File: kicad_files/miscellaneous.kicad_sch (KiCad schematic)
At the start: 28 parts, among them J2 TYPE-C-31-M-12, Q1 DTC123JKAT146, SW1 SW_SPST, SW2 EC11, U2 USBLC6-2SC6, U3 MCP1700-3302E

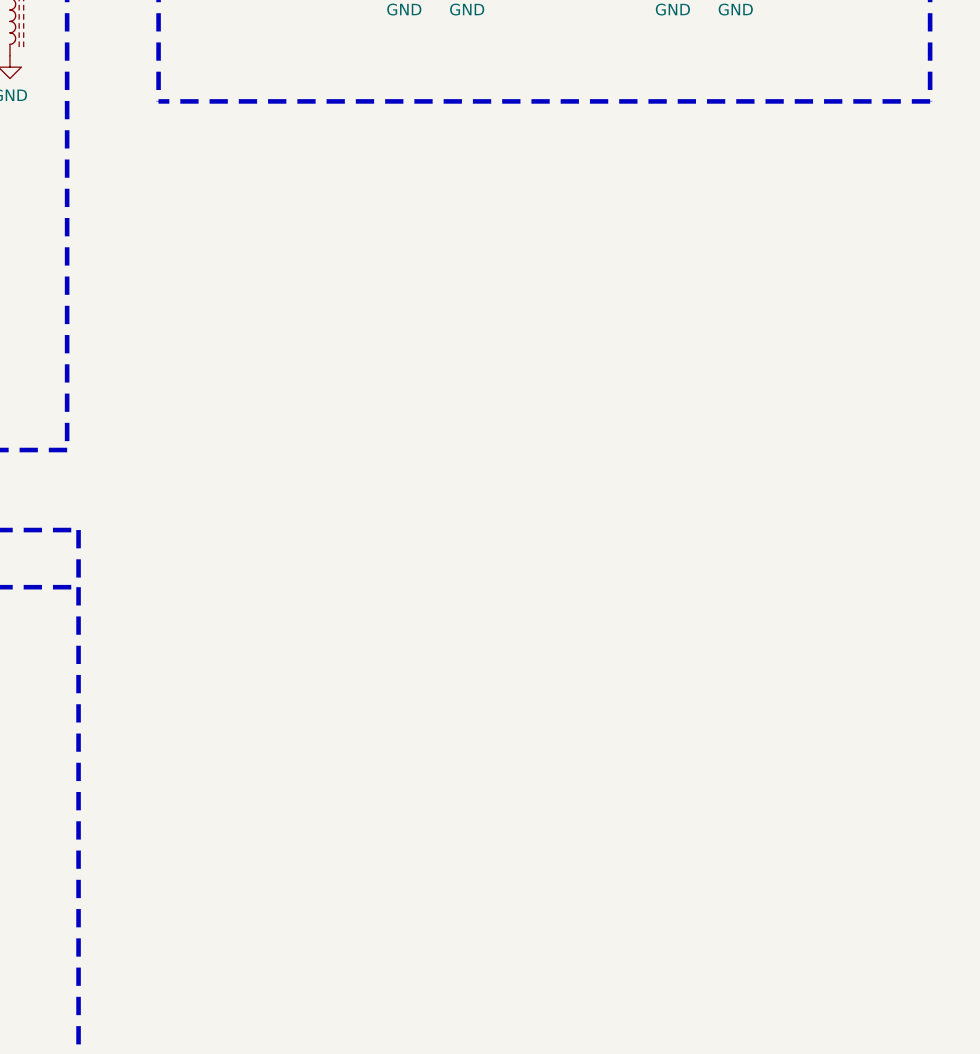
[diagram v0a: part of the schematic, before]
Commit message: Added mounting holes and jst connector
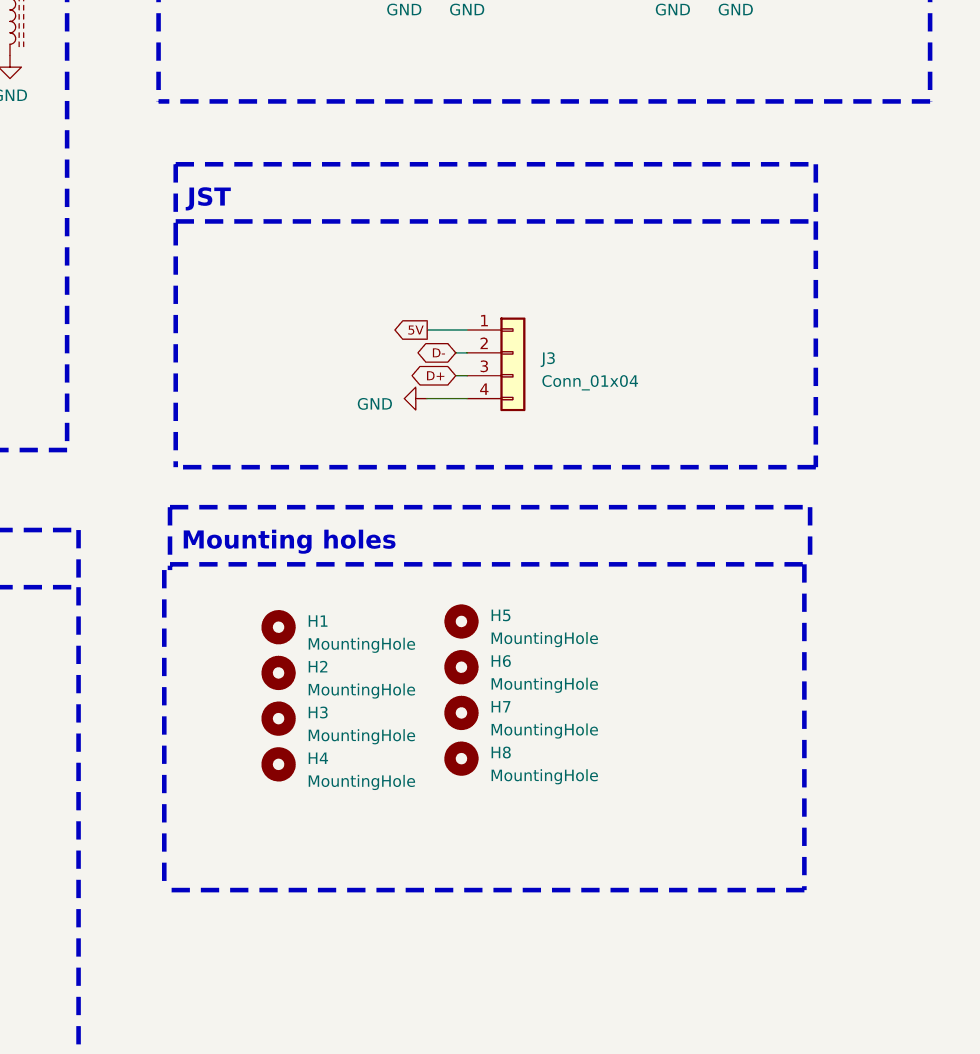
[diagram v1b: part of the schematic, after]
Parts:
- added H1, H2, H3, H4: MountingHole, acheron_MountingHoles:MountingHole_2.5x4.0mm, symbol Mechanical:MountingHole
- added H5, H6, H7, H8: MountingHole, acheron_MountingHoles:MoutingHole_Oval_7mm_5.0x2.5mm, symbol Mechanical:MountingHole
- added J3: Conn_01x04, acheron_Connectors:SM04B-SRSS-TB(LF)(SN)_mounting-reliefs, symbol Connector_Generic:Conn_01x04
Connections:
- net 5V: now also J3.1 (Pin_1)
- net D+: now also J3.3 (Pin_3)
- net D-: now also J3.2 (Pin_2)
- net GND: now also J3.4 (Pin_4)
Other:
- note added: "JST"
- note added: "Mounting holes"

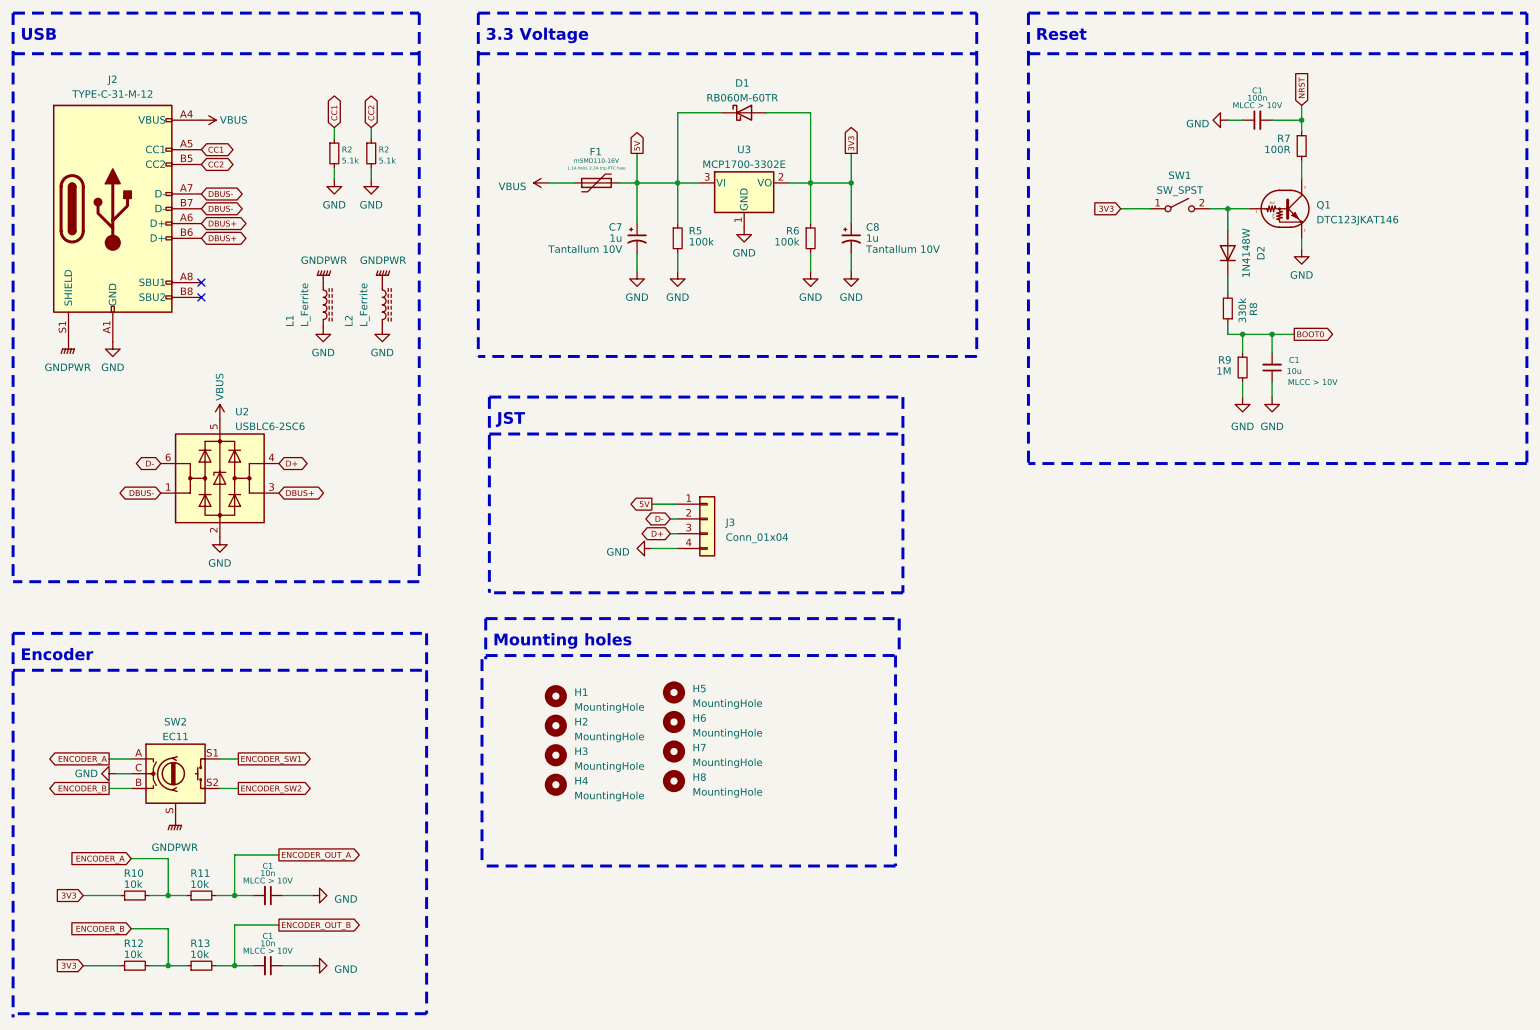
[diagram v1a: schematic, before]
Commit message: Added oled
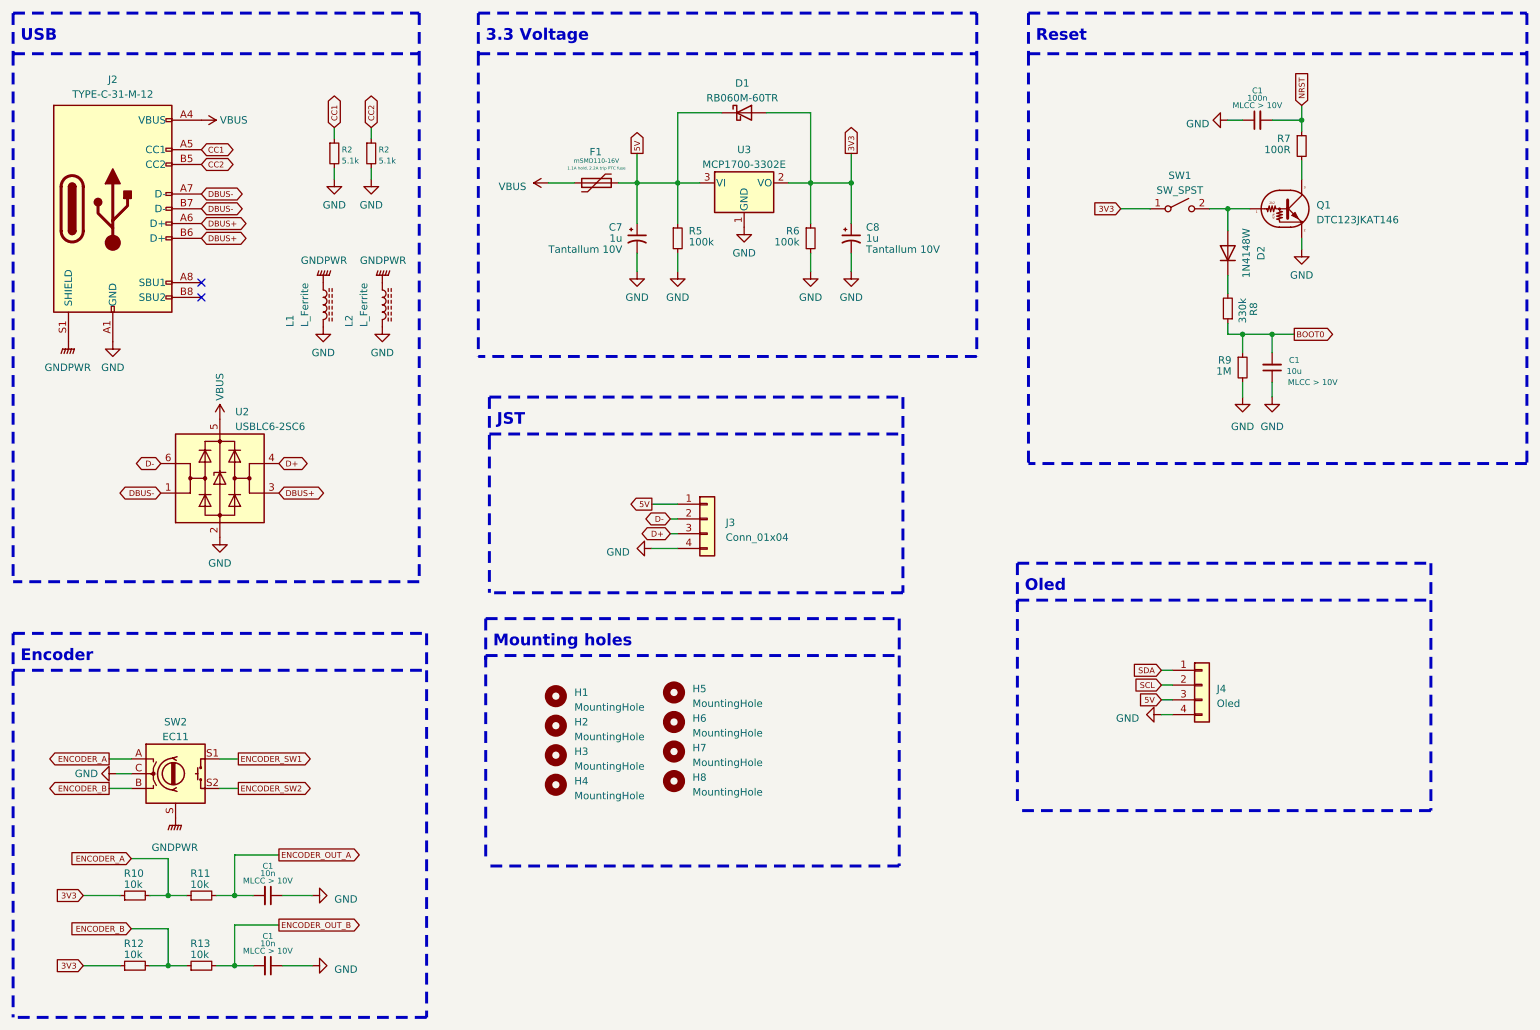
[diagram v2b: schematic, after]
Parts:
- added J4: Oled, acheron_Connectors:PinHeader_1x4_P2.54mm_Vertical, symbol Connector_Generic:Conn_01x04
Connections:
- net 5V: now also J4.3 (Pin_3)
- net GND: now also J4.4 (Pin_4)
- new net SCL: J4.2 (Pin_2)
- new net SDA: J4.1 (Pin_1)
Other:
- note added: "Oled"
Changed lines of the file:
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@@
   (no_connect (at 50.165 62.865))
   (no_connect (at 50.165 65.405))
+  (polyline (pts (xy 190.5 117.475) (xy 190.5 153.035))
+    (stroke (width 0.508) (type dash))
+  )
   (wire (pts (xy 64.135 168.275) (xy 69.215 168.275))
     (stroke (width 0) (type default))
@@
     (stroke (width 0.508) (type dash))
   )
-  (polyline (pts (xy 169.545 127) (xy 169.545 163.195))
+  (polyline (pts (xy 170.18 127) (xy 170.18 163.195))
     (stroke (width 0.508) (type dash))
   )
@@
     (stroke (width 0) (type default))
   )
-  (polyline (pts (xy 98.425 127.635) (xy 98.425 163.195))
+  (polyline (pts (xy 99.06 127) (xy 99.06 162.56))
     (stroke (width 0.508) (type dash))
   )
@@
     (stroke (width 0.508) (type dash))
   )
+  (polyline (pts (xy 261.62 111.125) (xy 261.62 117.475))
+    (stroke (width 0.508) (type dash))
+  )
   (polyline (pts (xy 99.06 120.65) (xy 170.18 120.65))
     (stroke (width 0.508) (type dash))
@@
     (stroke (width 0.508) (type dash))
   )
+  (polyline (pts (xy 261.62 153.67) (xy 190.5 153.67))
+    (stroke (width 0.508) (type dash))
+  )
   (wire (pts (xy 161.925 45.72) (xy 161.925 52.705))
     (stroke (width 0) (type default))
@@
     (stroke (width 0.508) (type dash))
   )
+  (wire (pts (xy 215.265 129.54) (xy 217.17 129.54))
+    (stroke (width 0) (type default))
+  )
   (wire (pts (xy 161.925 40.64) (xy 161.925 45.72))
     (stroke (width 0) (type default))
@@
     (stroke (width 0.508) (type dash))
   )
+  (polyline (pts (xy 190.5 111.125) (xy 190.5 118.11))
+    (stroke (width 0.508) (type dash))
+  )
   (wire (pts (xy 38.1 161.925) (xy 44.45 161.925))
     (stroke (width 0) (type default))
@@
     (stroke (width 0) (type default))
   )
+  (polyline (pts (xy 190.5 111.125) (xy 261.62 111.125))
+    (stroke (width 0.508) (type dash))
+  )
   (polyline (pts (xy 170.815 116.205) (xy 99.695 116.205))
     (stroke (width 0.508) (type dash))
@@
     (stroke (width 0.508) (type dash))
   )
+  (polyline (pts (xy 261.62 117.475) (xy 261.62 153.67))
+    (stroke (width 0.508) (type dash))
+  )
   (polyline (pts (xy 17.78 123.19) (xy 17.78 130.175))
     (stroke (width 0.508) (type dash))
@@
     (stroke (width 0) (type default))
   )
-  (polyline (pts (xy 169.545 163.195) (xy 98.425 163.195))
+  (polyline (pts (xy 170.18 163.195) (xy 99.06 163.195))
     (stroke (width 0.508) (type dash))
   )
@@
     (stroke (width 0) (type default))
   )
-  (polyline (pts (xy 88.9 129.54) (xy 88.9 188.595))
-    (stroke (width 0.508) (type dash))
+  (polyline (pts (xy 88.9 129.54) (xy 88.9 189.23))
+    (stroke (width 0.508) (type dash))
+  )
+  (wire (pts (xy 215.265 134.62) (xy 217.17 134.62))
+    (stroke (width 0) (type default))
   )
   (wire (pts (xy 234.315 34.925) (xy 239.395 34.925))
@@
     (stroke (width 0) (type default))
   )
+  (polyline (pts (xy 190.5 117.475) (xy 261.62 117.475))
+    (stroke (width 0.508) (type dash))
+  )
   (wire (pts (xy 55.88 168.275) (xy 55.88 161.29))
     (stroke (width 0) (type default))
@@
     (stroke (width 0) (type default))
   )
-  (polyline (pts (xy 88.9 188.595) (xy 17.78 188.595))
+  (polyline (pts (xy 88.9 189.23) (xy 17.78 189.23))
     (stroke (width 0.508) (type dash))
   )
@@
     (stroke (width 0) (type default))
   )
+  (wire (pts (xy 215.265 137.16) (xy 217.17 137.16))
+    (stroke (width 0) (type default))
+  )
   (polyline (pts (xy 99.06 120.65) (xy 99.06 127.635))
     (stroke (width 0.508) (type dash))
@@
   )
   (wire (pts (xy 73.025 36.195) (xy 73.025 38.1))
+    (stroke (width 0) (type default))
+  )
+  (wire (pts (xy 215.265 132.08) (xy 217.17 132.08))
     (stroke (width 0) (type default))
   )
@@
   )
   (text "Mounting holes" (at 100.33 125.73 0)
+    (effects (font (size 2 2) (thickness 1.524) bold) (justify left bottom))
+  )
+  (text "Oled" (at 191.77 116.205 0)
     (effects (font (size 2 2) (thickness 1.524) bold) (justify left bottom))
   )
@@
     )
   )
+  (global_label "SDA" (shape input) (at 215.265 129.54 180) (fields_autoplaced)
+    (effects (font (size 1 1)) (justify right))
+    (property "Intersheetrefs" "${INTERSHEET_REFS}" (at 210.0926 129.54 0)
+      (effects (font (size 1.27 1.27)) (justify right) hide)
+    )
+  )
   (global_label "BOOT0" (shape output) (at 238.125 71.755 0) (fields_autoplaced)
     (effects (font (size 1 1)) (justify left))
@@
     )
   )
+  (global_label "SCL" (shape input) (at 215.265 132.08 180) (fields_autoplaced)
+    (effects (font (size 1 1)) (justify right))
+    (property "Intersheetrefs" "${INTERSHEET_REFS}" (at 210.1402 132.08 0)
+      (effects (font (size 1.27 1.27)) (justify right) hide)
+    )
+  )
   (global_label "DBUS+" (shape bidirectional) (at 50.165 52.705 0) (fields_autoplaced)
     (effects (font (size 1 1)) (justify left))
@@
     )
   )
+  (global_label "5V" (shape input) (at 215.265 134.62 180) (fields_autoplaced)
+    (effects (font (size 1 1)) (justify right))
+    (property "Intersheetrefs" "${INTERSHEET_REFS}" (at 211.0926 134.62 0)
+      (effects (font (size 1.27 1.27)) (justify right) hide)
+    )
+  )
   (global_label "DBUS-" (shape bidirectional) (at 43.18 99.06 180) (fields_autoplaced)
     (effects (font (size 1 1)) (justify right))
@@
         (path "/9ce6b20d-0a6c-402a-b232-5eafd6242eb3/91dbea92-d93a-4a38-98ab-2a992bec1375"
           (reference "#PWR033") (unit 1)
+        )
+      )
+    )
+  )
+  (symbol (lib_id "power:GND") (at 215.265 137.16 270) (unit 1)
+    (in_bom yes) (on_board yes) (dnp no) (fields_autoplaced)
+    (property "Reference" "#PWR034" (at 208.915 137.16 0)
+      (effects (font (size 1.27 1.27)) hide)
+    )
+    (property "Value" "GND" (at 211.455 137.795 90)
+      (effects (font (size 1.27 1.27)) (justify right))
+    )
+    (property "Footprint" "" (at 215.265 137.16 0)
+      (effects (font (size 1.27 1.27)) hide)
+    )
+    (property "Datasheet" "" (at 215.265 137.16 0)
+      (effects (font (size 1.27 1.27)) hide)
+    )
+    (pin "1")
+    (instances
+      (project "Knobert_MacroPad"
+        (path "/9ce6b20d-0a6c-402a-b232-5eafd6242eb3/91dbea92-d93a-4a38-98ab-2a992bec1375"
+          (reference "#PWR034") (unit 1)
         )
       )
@@
         )
       )
+    )
+  )
+  (symbol (lib_id "Connector_Generic:Conn_01x04") (at 222.25 132.08 0) (unit 1)
+    (in_bom yes) (on_board yes) (dnp no) (fields_autoplaced)
+    (property "Reference" "J4" (at 224.79 132.715 0)
+      (effects (font (size 1.27 1.27)) (justify left))
+    )
+    (property "Value" "Oled" (at 224.79 135.255 0)
+      (effects (font (size 1.27 1.27)) (justify left))
+    )
+    (property "Footprint" "acheron_Connectors:PinHeader_1x4_P2.54mm_Vertical" (at 222.25 132.08 0)
+      (effects (font (size 1.27 1.27)) hide)
+    )
+    (property "Datasheet" "~" (at 222.25 132.08 0)
+      (effects (font (size 1.27 1.27)) hide)
+    )
+    (property "Package" "" (at 222.25 132.08 0)
+      (effects (font (size 1.27 1.27)) hide)
+    )
+    (property "Manufacturer" "" (at 222.25 132.08 0)
+      (effects (font (size 1.27 1.27)) hide)
+    )
+    (property "Manufacturer Part Number" "" (at 222.25 132.08 0)
+      (effects (font (size 1.27 1.27)) hide)
+    )
+    (property "Vendor Part Number" "" (at 222.25 132.08 0)
+      (effects (font (size 1.27 1.27)) hide)
+    )
+    (property "Description" "" (at 222.25 132.08 0)
+      (effects (font (size 1.27 1.27)) hide)
+    )
+    (pin "1")
+    (pin "2")
+    (pin "3")
+    (pin "4")
+    (instances
+      (project "Knobert_MacroPad"
+        (path "/9ce6b20d-0a6c-402a-b232-5eafd6242eb3/91dbea92-d93a-4a38-98ab-2a992bec1375"
+          (reference "J4") (unit 1)
+        )
+      )

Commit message: beta pcb layout
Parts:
- removed H7, H8: MountingHole, acheron_MountingHoles:MoutingHole_Oval_7mm_5.0x2.5mm, symbol Mechanical:MountingHole
- added H9: MountingHole, acheron_Graphics:OSH_Logo_22.5x8.5mm, symbol Mechanical:MountingHole
- C1: footprint acheron_Components:C_0402_1005Metric -> Capacitor_SMD:C_0805_2012Metric
- C23: renamed from C7; footprint acheron_Components:CP_EIA-3216-10_Kemet-I_Pad1.58x1.35mm_HandSolder -> Capacitor_SMD:C_0805_2012Metric
- C24: renamed from C8; footprint acheron_Components:CP_EIA-3216-10_Kemet-I_Pad1.58x1.35mm_HandSolder -> Capacitor_SMD:C_0805_2012Metric
- H5, H6: footprint acheron_MountingHoles:MoutingHole_Oval_7mm_5.0x2.5mm -> acheron_Hardware:MouseBite_IPC7351
- R15: renamed from R10; footprint acheron_Components:R_0402_1005Metric -> Resistor_SMD:R_0805_2012Metric
- R16: renamed from R12; footprint acheron_Components:R_0402_1005Metric -> Resistor_SMD:R_0805_2012Metric
- R17: renamed from R11; footprint acheron_Components:R_0402_1005Metric -> Resistor_SMD:R_0805_2012Metric
- R18: renamed from R13; footprint acheron_Components:R_0402_1005Metric -> Resistor_SMD:R_0805_2012Metric
- R2: footprint acheron_Components:R_0402_1005Metric -> Resistor_SMD:R_0805_2012Metric
- R21: renamed from R5; footprint acheron_Components:R_0402_1005Metric -> Resistor_SMD:R_0805_2012Metric
- R22: renamed from R6; footprint acheron_Components:R_0402_1005Metric -> Resistor_SMD:R_0805_2012Metric
- R23: renamed from R8; footprint acheron_Components:R_0402_1005Metric -> Resistor_SMD:R_0805_2012Metric
- R24: renamed from R9; footprint acheron_Components:R_0402_1005Metric -> Resistor_SMD:R_0805_2012Metric
- R25: renamed from R7; footprint acheron_Components:R_0402_1005Metric -> Resistor_SMD:R_0805_2012Metric
- SW13: renamed from SW2; footprint (none) -> acheron_Hardware:ALPS_EC11E
- renumbered D1 to D26, D2 to D27, SW1 to SW14
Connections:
- net 5V: now also J4.2 (Pin_2); no longer J4.3 (Pin_3)
- net GND: now also J4.1 (Pin_1); no longer J4.4 (Pin_4)
- net SCL: now also J4.3 (Pin_3); no longer J4.2 (Pin_2)
- net SDA: now also J4.4 (Pin_4); no longer J4.1 (Pin_1)
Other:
- note added: "Mounting holes/Graphics"
- note removed: "Mounting holes"
